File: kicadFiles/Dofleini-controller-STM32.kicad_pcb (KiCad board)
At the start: 2 copper layers, 89 x 31 mm, 32 parts, among them J1 Conn_ARM_JTAG_SWD_10, J2 Conn_01x09_Male, J3 TYPE-C-31-M12_13, J4 Conn_01x22_Male, J5 Conn_01x07_Male, Q1 DTC123J, Q2 AO4406AL, U1 STM32F072CBTx, U2 TLV1117-33, U3 USBLC6-2SC6

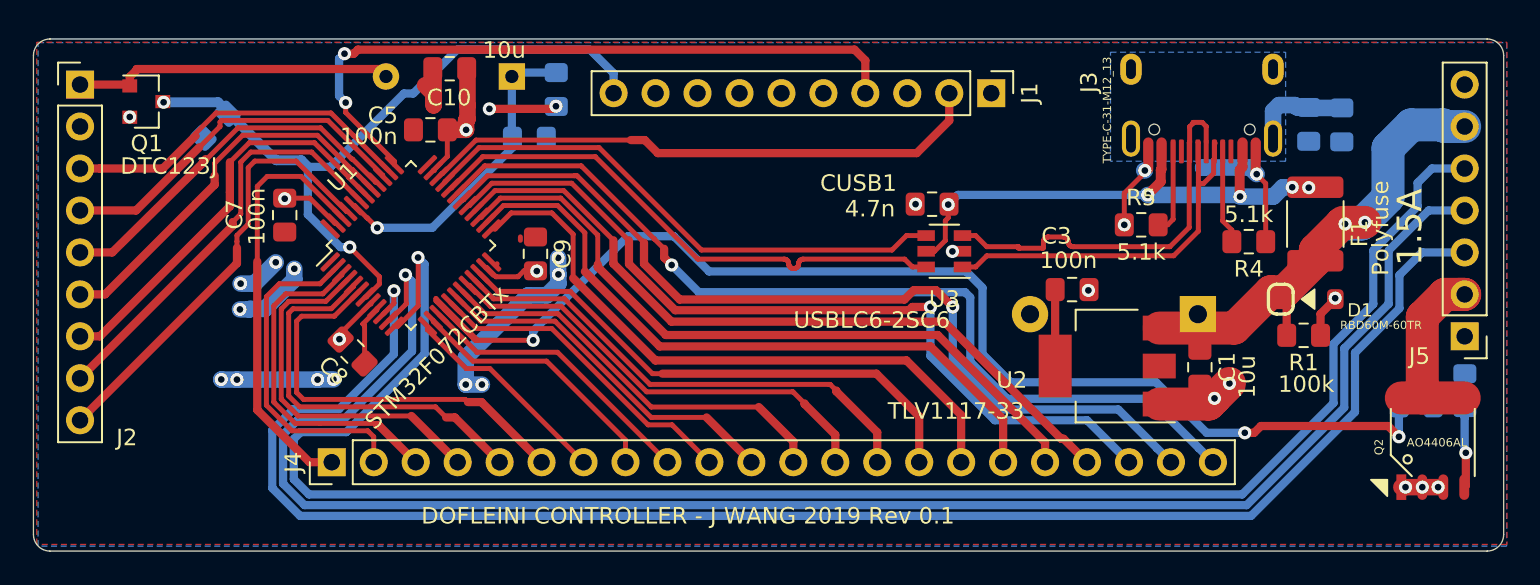
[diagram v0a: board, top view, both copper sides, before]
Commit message: Added mounting holes
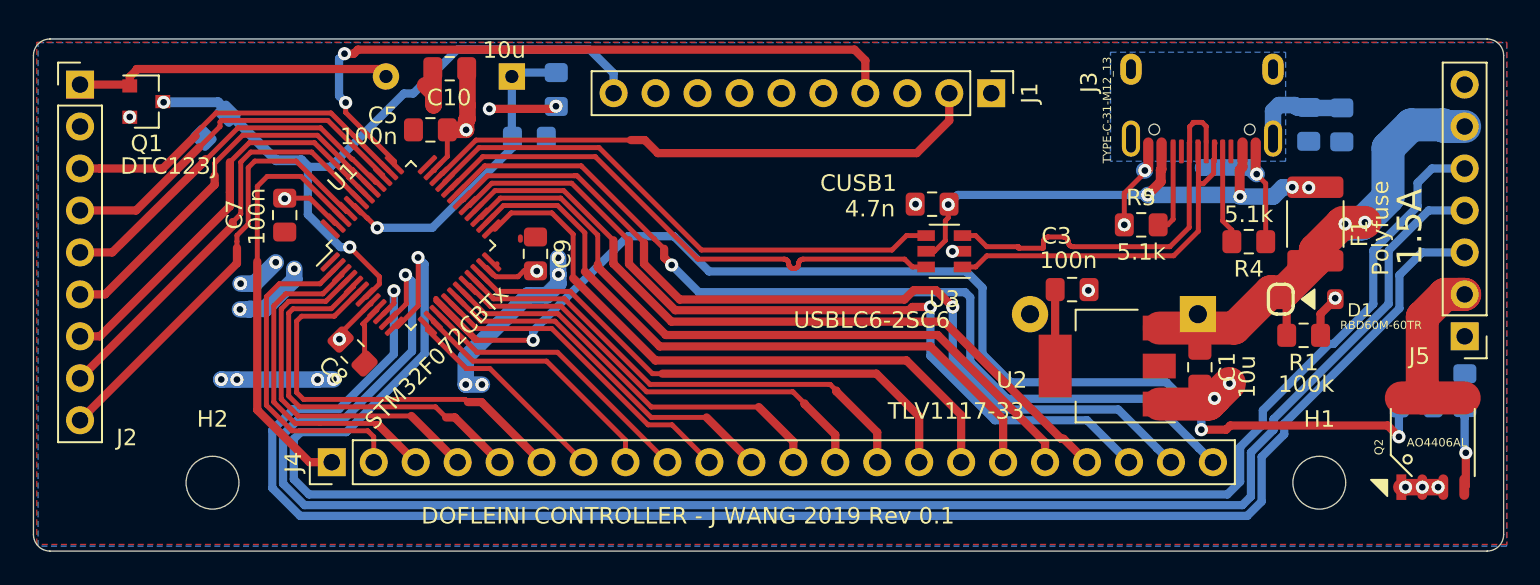
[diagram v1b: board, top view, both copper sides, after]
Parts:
- added H1: MountingHole, MountingHole:MountingHole_3.2mm_M3_ISO7380, F.Cu at (31.8, 8.86)
- added H2: MountingHole, MountingHole:MountingHole_3.2mm_M3_ISO7380, F.Cu at (-35.2, 8.86)
- R7: value 100 -> 10k
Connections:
- J1 pad 6: Net-(J1-Pad6) -> (no net)
- J1 pad 7: Net-(J1-Pad7) -> (no net)
- J1 pad 8: Net-(J1-Pad8) -> (no net)
- J3 pad A8: Net-(J3-PadA8) -> (no net)
- J3 pad B8: Net-(J3-PadB8) -> (no net)
